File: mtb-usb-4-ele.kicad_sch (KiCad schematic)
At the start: 76 parts, among them J1 USB_C_Receptacle_USB2.0, J2 PROG/DEBUG, J3 Conn_01x06, J4 RJ12, J5 RJ12, J6 Screw_Terminal_01x02, J7 Screw_Terminal_01x02, J8 Conn_01x02, U1 STM32F103C8Tx, U2 AMS1117-3.3, U3 ADM2483xRW, U4 ADUM1250, U6 LM78M05_TO252, U7 INA219AxDCN, Y1 8 MHz

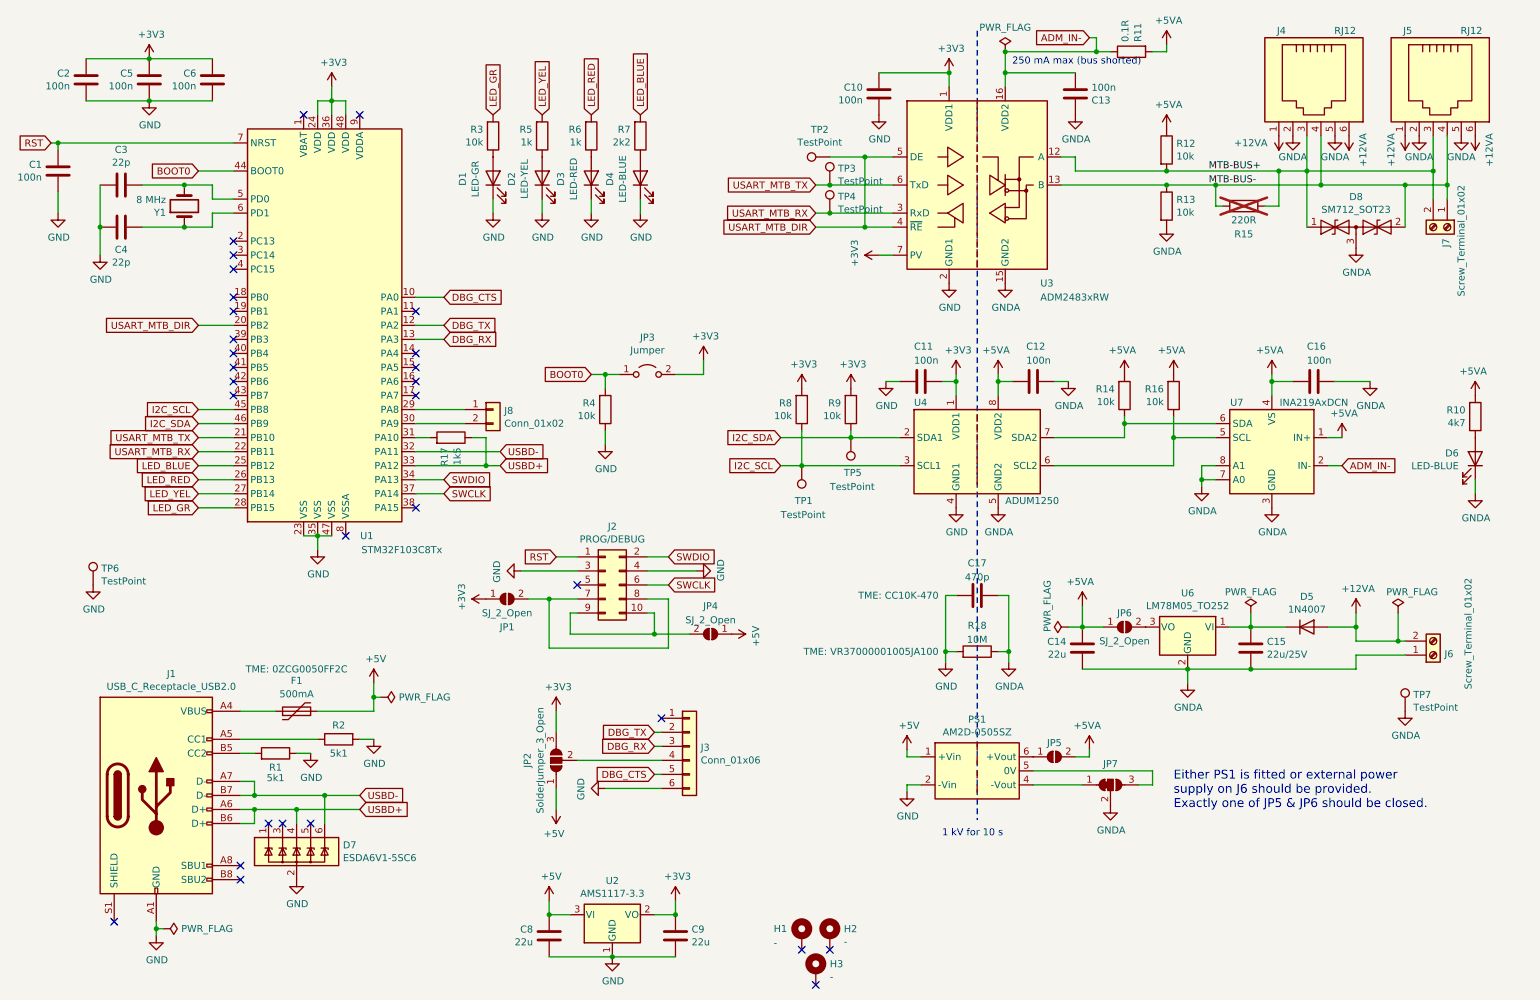
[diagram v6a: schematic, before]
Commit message: Screw terminals: use exact part value.
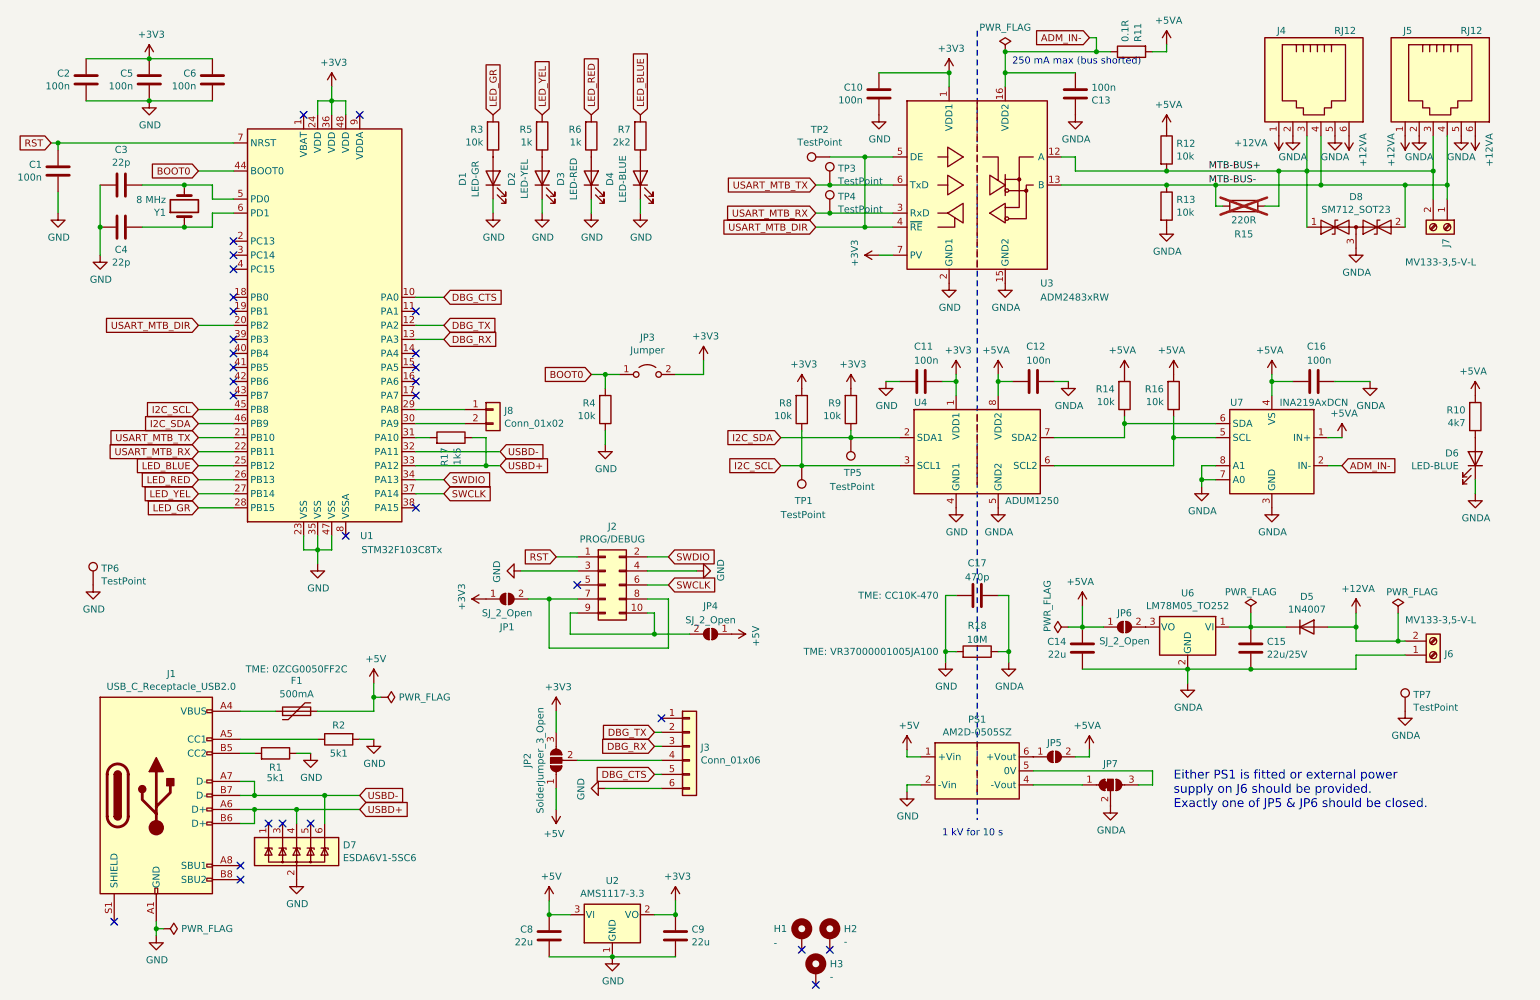
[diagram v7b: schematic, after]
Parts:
- J6, J7: value Screw_Terminal_01x02 -> MV133-3,5-V-L
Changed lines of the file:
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@@
 	)
 	(junction
-		(at 68.58 107.95)
+		(at 68.58 110.49)
 		(diameter 0)
 		(color 0 0 0 0)
@@
 	(wire
 		(pts
-			(xy 68.58 107.95) (xy 71.12 107.95)
+			(xy 68.58 110.49) (xy 71.12 110.49)
 		)
 		(stroke
@@
 	(wire
 		(pts
+			(xy 66.04 110.49) (xy 66.04 107.95)
+		)
+		(stroke
+			(width 0)
+			(type default)
+		)
+	)
+	(wire
+		(pts
 			(xy 57.15 152.4) (xy 54.61 152.4)
 		)
@@
 	(wire
 		(pts
+			(xy 68.58 110.49) (xy 68.58 107.95)
+		)
+		(stroke
+			(width 0)
+			(type default)
+		)
+	)
+	(wire
+		(pts
 			(xy 49.53 49.53) (xy 53.34 49.53)
 		)
@@
 	(wire
 		(pts
-			(xy 68.58 110.49) (xy 68.58 107.95)
+			(xy 68.58 113.03) (xy 68.58 110.49)
 		)
 		(stroke
@@
 	(wire
 		(pts
-			(xy 66.04 107.95) (xy 68.58 107.95)
+			(xy 66.04 110.49) (xy 68.58 110.49)
 		)
 		(stroke
@@
 	(wire
 		(pts
+			(xy 71.12 110.49) (xy 71.12 107.95)
+		)
+		(stroke
+			(width 0)
+			(type default)
+		)
+	)
+	(wire
+		(pts
 			(xy 21.59 38.1) (xy 21.59 36.83)
 		)
@@
 			)
 		)
-		(property "Value" "Screw_Terminal_01x02"
-			(at 275.59 44.45 0)
+		(property "Value" "MV133-3,5-V-L"
+			(at 265.43 58.42 90)
 			(effects
 				(font
@@
 			)
 		)
-		(property "Value" "Screw_Terminal_01x02"
-			(at 276.86 115.57 90)
+		(property "Value" "MV133-3,5-V-L"
+			(at 265.43 123.19 0)
 			(effects
 				(font
@@
 	(symbol
 		(lib_id "power:GND")
-		(at 68.58 110.49 0)
+		(at 68.58 113.03 0)
 		(unit 1)
 		(exclude_from_sim no)
@@
 		(dnp no)
 		(property "Reference" "#PWR08"
-			(at 68.58 116.84 0)
+			(at 68.58 119.38 0)
 			(effects
 				(font
@@
 		)
 		(property "Value" "GND"
-			(at 68.707 114.8842 0)
+			(at 68.707 117.4242 0)
 			(effects
 				(font
@@
 		)
 		(property "Footprint" ""
-			(at 68.58 110.49 0)
+			(at 68.58 113.03 0)
 			(effects
 				(font
@@
 		)
 		(property "Datasheet" ""
-			(at 68.58 110.49 0)
+			(at 68.58 113.03 0)
 			(effects
 				(font
@@
 		)
 		(property "Description" ""
-			(at 68.58 110.49 0)
+			(at 68.58 113.03 0)
 			(effects
 				(font

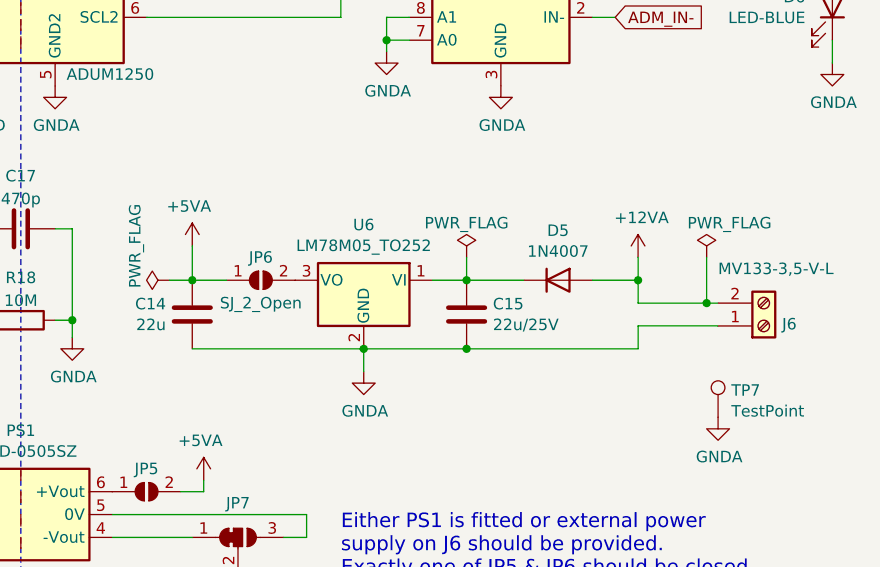
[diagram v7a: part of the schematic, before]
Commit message: Add fuse F2 for MTBbus power.
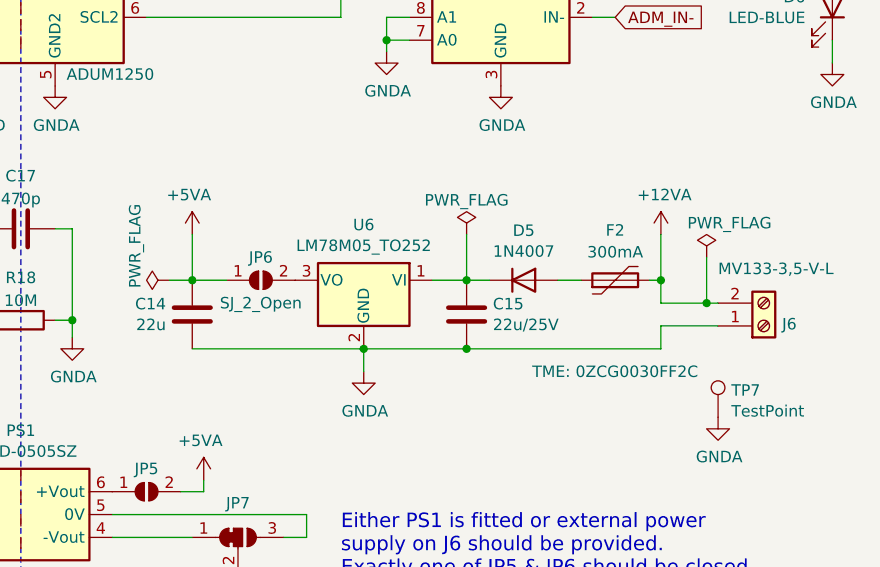
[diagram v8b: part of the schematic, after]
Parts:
- added F2: 300mA, Fuse:Fuse_1812_4532Metric, symbol Device:Polyfuse
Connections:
- net +12VA: now also F2.2; no longer D5.2 (A)
- new net: D5.2 (A), F2.1
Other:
- moved on the sheet: D5
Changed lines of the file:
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@@
 	)
 	(junction
-		(at 256.54 124.46)
+		(at 259.08 124.46)
 		(diameter 0)
 		(color 0 0 0 0)
@@
 	(wire
 		(pts
+			(xy 257.81 124.46) (xy 259.08 124.46)
+		)
+		(stroke
+			(width 0)
+			(type default)
+		)
+	)
+	(wire
+		(pts
 			(xy 68.58 29.21) (xy 71.12 29.21)
 		)
@@
 	(wire
 		(pts
-			(xy 256.54 127) (xy 264.16 127)
+			(xy 259.08 127) (xy 264.16 127)
 		)
 		(stroke
@@
 	(wire
 		(pts
-			(xy 237.49 124.46) (xy 243.84 124.46)
+			(xy 237.49 124.46) (xy 240.03 124.46)
 		)
 		(stroke
@@
 	(wire
 		(pts
-			(xy 256.54 124.46) (xy 256.54 127)
+			(xy 259.08 124.46) (xy 259.08 127)
 		)
 		(stroke
@@
 	(wire
 		(pts
-			(xy 256.54 121.92) (xy 256.54 124.46)
+			(xy 259.08 119.38) (xy 259.08 124.46)
 		)
 		(stroke
@@
 	(wire
 		(pts
-			(xy 237.49 121.92) (xy 237.49 124.46)
+			(xy 237.49 119.38) (xy 237.49 124.46)
 		)
 		(stroke
@@
 	(wire
 		(pts
-			(xy 207.01 120.65) (xy 207.01 124.46)
+			(xy 207.01 119.38) (xy 207.01 124.46)
 		)
 		(stroke
@@
 	(wire
 		(pts
-			(xy 251.46 124.46) (xy 256.54 124.46)
-		)
-		(stroke
-			(width 0)
-			(type default)
-		)
-	)
-	(wire
-		(pts
 			(xy 250.19 44.45) (xy 265.43 44.45)
 		)
@@
 	(wire
 		(pts
-			(xy 256.54 129.54) (xy 256.54 132.08)
+			(xy 259.08 129.54) (xy 259.08 132.08)
 		)
 		(stroke
@@
 	(wire
 		(pts
-			(xy 256.54 129.54) (xy 265.43 129.54)
+			(xy 259.08 129.54) (xy 265.43 129.54)
 		)
 		(stroke
@@
 	(wire
 		(pts
+			(xy 247.65 124.46) (xy 250.19 124.46)
+		)
+		(stroke
+			(width 0)
+			(type default)
+		)
+	)
+	(wire
+		(pts
 			(xy 184.15 80.01) (xy 184.15 82.55)
 		)
@@
 	(wire
 		(pts
-			(xy 237.49 132.08) (xy 256.54 132.08)
+			(xy 237.49 132.08) (xy 259.08 132.08)
 		)
 		(stroke
@@
 	(symbol
 		(lib_id "power:+5VA")
-		(at 207.01 120.65 0)
+		(at 207.01 119.38 0)
 		(mirror y)
 		(unit 1)
@@
 		(dnp no)
 		(property "Reference" "#PWR045"
-			(at 207.01 124.46 0)
+			(at 207.01 123.19 0)
 			(effects
 				(font
@@
 		)
 		(property "Value" "+5VA"
-			(at 206.629 116.2558 0)
+			(at 206.629 114.9858 0)
 			(effects
 				(font
@@
 		)
 		(property "Footprint" ""
-			(at 207.01 120.65 0)
+			(at 207.01 119.38 0)
 			(effects
 				(font
@@
 		)
 		(property "Datasheet" ""
-			(at 207.01 120.65 0)
+			(at 207.01 119.38 0)
 			(effects
 				(font
@@
 		)
 		(property "Description" ""
-			(at 207.01 120.65 0)
+			(at 207.01 119.38 0)
 			(effects
 				(font
@@
 	(symbol
 		(lib_id "power:PWR_FLAG")
-		(at 237.49 121.92 0)
+		(at 237.49 119.38 0)
 		(unit 1)
 		(exclude_from_sim no)
@@
 		(dnp no)
 		(property "Reference" "#FLG03"
-			(at 237.49 120.015 0)
+			(at 237.49 117.475 0)
 			(effects
 				(font
@@
 		)
 		(property "Value" "PWR_FLAG"
-			(at 237.49 118.11 0)
+			(at 237.49 115.57 0)
 			(effects
 				(font
@@
 		)
 		(property "Footprint" ""
-			(at 237.49 121.92 0)
+			(at 237.49 119.38 0)
 			(effects
 				(font
@@
 		)
 		(property "Datasheet" "~"
-			(at 237.49 121.92 0)
+			(at 237.49 119.38 0)
 			(effects
 				(font
@@
 		)
 		(property "Description" ""
-			(at 237.49 121.92 0)
+			(at 237.49 119.38 0)
 			(effects
 				(font
@@
 	(symbol
 		(lib_id "power:+12VA")
-		(at 256.54 121.92 0)
+		(at 259.08 119.38 0)
 		(unit 1)
 		(exclude_from_sim no)
@@
 		(dnp no)
 		(property "Reference" "#PWR058"
-			(at 256.54 125.73 0)
+			(at 259.08 123.19 0)
 			(effects
 				(font
@@
 		)
 		(property "Value" "+12VA"
-			(at 256.921 117.5258 0)
+			(at 259.461 114.9858 0)
 			(effects
 				(font
@@
 		)
 		(property "Footprint" ""
-			(at 256.54 121.92 0)
+			(at 259.08 119.38 0)
 			(effects
 				(font
@@
 		)
 		(property "Datasheet" ""
-			(at 256.54 121.92 0)
+			(at 259.08 119.38 0)
 			(effects
 				(font
@@
 		)
 		(property "Description" ""
-			(at 256.54 121.92 0)
+			(at 259.08 119.38 0)
 			(effects
 				(font
@@
 	(symbol
 		(lib_id "Device:D")
-		(at 247.65 124.46 0)
+		(at 243.84 124.46 0)
 		(unit 1)
 		(exclude_from_sim no)
@@
 		(dnp no)
 		(property "Reference" "D5"
-			(at 247.65 118.9482 0)
+			(at 243.84 118.9482 0)
 			(effects
 				(font
@@
 		)
 		(property "Value" "1N4007"
-			(at 247.65 121.2596 0)
+			(at 243.84 121.2596 0)
 			(effects
 				(font
@@
 		)
 		(property "Footprint" "Diode_SMD:D_SOD-123"
-			(at 247.65 124.46 0)
+			(at 243.84 124.46 0)
 			(effects
 				(font
@@
 		)
 		(property "Datasheet" "~"
-			(at 247.65 124.46 0)
+			(at 243.84 124.46 0)
 			(effects
 				(font
@@
 		)
 		(property "Description" ""
-			(at 247.65 124.46 0)
+			(at 243.84 124.46 0)
 			(effects
 				(font
@@
 		)
 		(property "LCSC" "C64898"
-			(at 247.65 124.46 0)
+			(at 243.84 124.46 0)
 			(effects
 				(font
@@
 					(unit 1)
 				)
+			)
+		)
+	)
+	(symbol
+		(lib_id "Device:Polyfuse")
+		(at 254 124.46 90)
+		(unit 1)
+		(exclude_from_sim no)
+		(in_bom yes)
+		(on_board yes)
+		(dnp no)
+		(property "Reference" "F2"
+			(at 254 118.9185 90)
+			(effects
+				(font
+					(size 1.27 1.27)
+				)
+			)
+		)
+		(property "Value" "300mA"
+			(at 254 121.3428 90)
+			(effects
+				(font
+					(size 1.27 1.27)
+				)
+			)
+		)
+		(property "Footprint" "Fuse:Fuse_1812_4532Metric"
+			(at 259.08 123.19 0)
+			(effects
+				(font
+					(size 1.27 1.27)
+				)
+				(justify left)
+				(hide yes)
+			)
+		)
+		(property "Datasheet" "~"
+			(at 254 124.46 0)
+			(effects
+				(font
+					(size 1.27 1.27)
+				)
+				(hide yes)
+			)
+		)
+		(property "Description" "Resettable fuse, polymeric positive temperature coefficient"
+			(at 254 124.46 0)
+			(effects
+				(font
+					(size 1.27 1.27)
+				)
+				(hide yes)
+			)
+		)
+		(property "TME" "0ZCG0030FF2C"
+			(at 254 134.62 90)
+			(show_name yes)
+			(effects
+				(font
+					(size 1.27 1.27)
+				)
+			)
+		)
+		(pin "2"
+		)
+		(pin "1"
+		)
+		(instances
+			(project "mtb-usb-4-ele"
+				(path "/844d7d7a-b386-45a8-aaf6-bf41bbcb43b5"
+					(reference "F2")
+					(unit 1)
+				)
